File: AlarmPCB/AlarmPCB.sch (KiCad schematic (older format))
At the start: 13 parts

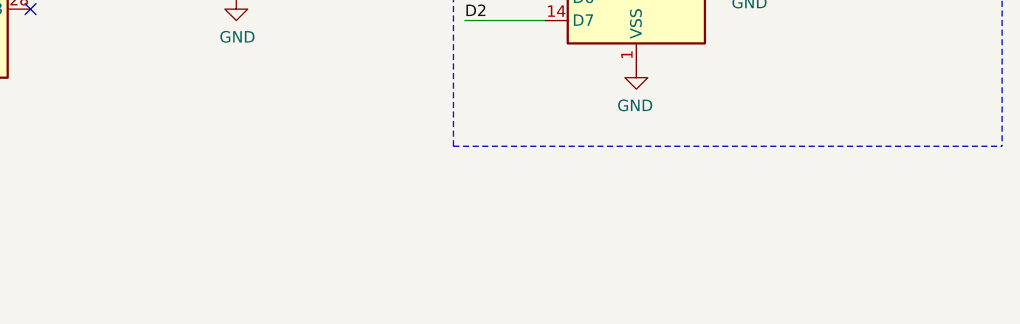
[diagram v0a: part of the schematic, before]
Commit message: Updated PCB GND Layer
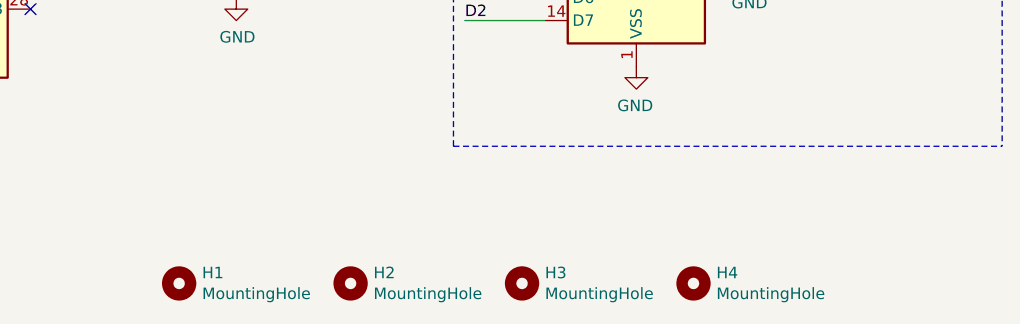
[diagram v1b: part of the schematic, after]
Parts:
- added H1, H2, H3, H4: MountingHole, MountingHole:MountingHole_3.2mm_M3, symbol Mechanical:MountingHole
- PB1: footprint Button_Switch_THT:SW_TH_Tactile_Omron_B3F-10xx -> Button_Switch_THT:SW_PUSH-12mm_Wuerth-430476085716
- PB2, PB3: footprint Button_Switch_THT:Push_E-Switch_KS01Q01 -> Button_Switch_THT:SW_TH_Tactile_Omron_B3F-10xx
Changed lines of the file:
@@
 EESchema Schematic File Version 4
-LIBS:AlarmPCB-cache
 EELAYER 30 0
 EELAYER END
@@
 F 0 "PB3" V 1900 3900 50  0000 C CNN
 F 1 "CancelAlarm" H 1500 3850 50  0000 C CNN
-F 2 "Button_Switch_THT:Push_E-Switch_KS01Q01" H 1750 3950 50  0001 C CNN
+F 2 "Button_Switch_THT:SW_TH_Tactile_Omron_B3F-10xx" H 1750 3950 50  0001 C CNN
 F 3 "~" H 1750 3950 50  0001 C CNN
 	1    1750 3750
@@
 F 0 "PB2" V 1500 3850 50  0000 C CNN
 F 1 "Snooze" H 1200 3850 50  0000 C CNN
-F 2 "Button_Switch_THT:Push_E-Switch_KS01Q01" H 1350 3950 50  0001 C CNN
+F 2 "Button_Switch_THT:SW_TH_Tactile_Omron_B3F-10xx" H 1350 3950 50  0001 C CNN
 F 3 "~" H 1350 3950 50  0001 C CNN
 	1    1350 3750
@@
 F 0 "PB1" V 1150 3850 50  0000 C CNN
 F 1 "Backlight" H 800 3850 50  0000 C CNN
-F 2 "Button_Switch_THT:SW_TH_Tactile_Omron_B3F-10xx" H 1000 3950 50  0001 C CNN
+F 2 "Button_Switch_THT:SW_PUSH-12mm_Wuerth-430476085716" H 1000 3950 50  0001 C CNN
 F 3 "~" H 1000 3950 50  0001 C CNN
 	1    1000 3750
@@
 NoConn ~ 8000 4100
 NoConn ~ 8000 4200
+$Comp
+L Mechanical:MountingHole H1
+U 1 1 5F1B765B
+P 6400 5750
+F 0 "H1" H 6500 5796 50  0000 L CNN
+F 1 "MountingHole" H 6500 5705 50  0000 L CNN
+F 2 "MountingHole:MountingHole_3.2mm_M3" H 6400 5750 50  0001 C CNN
+F 3 "~" H 6400 5750 50  0001 C CNN
+	1    6400 5750
+	1    0    0    -1
+$EndComp
+$Comp
+L Mechanical:MountingHole H2
+U 1 1 5F1B83F1
+P 7150 5750
+F 0 "H2" H 7250 5796 50  0000 L CNN
+F 1 "MountingHole" H 7250 5705 50  0000 L CNN
+F 2 "MountingHole:MountingHole_3.2mm_M3" H 7150 5750 50  0001 C CNN
+F 3 "~" H 7150 5750 50  0001 C CNN
+	1    7150 5750
+	1    0    0    -1
+$EndComp
+$Comp
+L Mechanical:MountingHole H3
+U 1 1 5F1BA130
+P 7900 5750
+F 0 "H3" H 8000 5796 50  0000 L CNN
+F 1 "MountingHole" H 8000 5705 50  0000 L CNN
+F 2 "MountingHole:MountingHole_3.2mm_M3" H 7900 5750 50  0001 C CNN
+F 3 "~" H 7900 5750 50  0001 C CNN
+	1    7900 5750
+	1    0    0    -1
+$EndComp
+$Comp
+L Mechanical:MountingHole H4
+U 1 1 5F1BA136
+P 8650 5750
+F 0 "H4" H 8750 5796 50  0000 L CNN
+F 1 "MountingHole" H 8750 5705 50  0000 L CNN
+F 2 "MountingHole:MountingHole_3.2mm_M3" H 8650 5750 50  0001 C CNN
+F 3 "~" H 8650 5750 50  0001 C CNN
+	1    8650 5750
+	1    0    0    -1
+$EndComp
 $EndSCHEMATC

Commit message: PCB Dimensions
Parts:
- PB1: footprint Button_Switch_THT:SW_PUSH-12mm_Wuerth-430476085716 -> Connector_PinHeader_2.54mm:PinHeader_1x03_P2.54mm_Vertical
- PB2, PB3: footprint Button_Switch_THT:SW_TH_Tactile_Omron_B3F-10xx -> Connector_PinHeader_2.54mm:PinHeader_1x02_P2.54mm_Vertical
- R1: footprint OptoDevice:R_LDR_4.9x4.2mm_P2.54mm_Vertical -> Connector_PinHeader_2.54mm:PinHeader_1x02_P2.54mm_Vertical
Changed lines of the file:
@@
 F 0 "PB3" V 1900 3900 50  0000 C CNN
 F 1 "CancelAlarm" H 1500 3850 50  0000 C CNN
-F 2 "Button_Switch_THT:SW_TH_Tactile_Omron_B3F-10xx" H 1750 3950 50  0001 C CNN
+F 2 "Connector_PinHeader_2.54mm:PinHeader_1x02_P2.54mm_Vertical" H 1750 3950 50  0001 C CNN
 F 3 "~" H 1750 3950 50  0001 C CNN
 	1    1750 3750
@@
 F 0 "PB2" V 1500 3850 50  0000 C CNN
 F 1 "Snooze" H 1200 3850 50  0000 C CNN
-F 2 "Button_Switch_THT:SW_TH_Tactile_Omron_B3F-10xx" H 1350 3950 50  0001 C CNN
+F 2 "Connector_PinHeader_2.54mm:PinHeader_1x02_P2.54mm_Vertical" H 1350 3950 50  0001 C CNN
 F 3 "~" H 1350 3950 50  0001 C CNN
 	1    1350 3750
@@
 F 0 "PB1" V 1150 3850 50  0000 C CNN
 F 1 "Backlight" H 800 3850 50  0000 C CNN
-F 2 "Button_Switch_THT:SW_PUSH-12mm_Wuerth-430476085716" H 1000 3950 50  0001 C CNN
+F 2 "Connector_PinHeader_2.54mm:PinHeader_1x03_P2.54mm_Vertical" H 1000 3950 50  0001 C CNN
 F 3 "~" H 1000 3950 50  0001 C CNN
 	1    1000 3750
@@
 F 0 "R1" V 4150 2950 50  0000 L CNN
 F 1 "PhotoResistor" V 4250 2800 50  0000 L CNN
-F 2 "OptoDevice:R_LDR_4.9x4.2mm_P2.54mm_Vertical" V 4100 2750 50  0001 L CNN
+F 2 "Connector_PinHeader_2.54mm:PinHeader_1x02_P2.54mm_Vertical" V 4100 2750 50  0001 L CNN
 F 3 "~" H 4050 2950 50  0001 C CNN
 	1    4050 3000

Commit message: Updated Pot footprint
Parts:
- RV1: footprint Potentiometer_THT:Potentiometer_ACP_CA6-H2,5_Horizontal -> digikey-footprints:Potentiometer_P120PK-Y25BR10K
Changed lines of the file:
@@
 EESchema Schematic File Version 4
+LIBS:AlarmPCB-cache
 EELAYER 30 0
 EELAYER END
@@
 F 0 "RV1" V 9300 3450 50  0000 R CNN
 F 1 "Contrast" H 9350 3550 50  0000 R CNN
-F 2 "Potentiometer_THT:Potentiometer_ACP_CA6-H2,5_Horizontal" H 9400 3400 50  0001 C CNN
+F 2 "digikey-footprints:Potentiometer_P120PK-Y25BR10K" H 9400 3400 50  0001 C CNN
 F 3 "~" H 9400 3400 50  0001 C CNN
 	1    9400 3400

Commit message: PCB rev
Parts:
- PB1: footprint Connector_PinHeader_2.54mm:PinHeader_1x03_P2.54mm_Vertical -> Button_Switch_THT:SW_TH_Tactile_Omron_B3F-10xx
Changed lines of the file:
@@
 EESchema Schematic File Version 4
-LIBS:AlarmPCB-cache
 EELAYER 30 0
 EELAYER END
@@
 F 0 "PB1" V 1150 3850 50  0000 C CNN
 F 1 "Backlight" H 800 3850 50  0000 C CNN
-F 2 "Connector_PinHeader_2.54mm:PinHeader_1x03_P2.54mm_Vertical" H 1000 3950 50  0001 C CNN
+F 2 "Button_Switch_THT:SW_TH_Tactile_Omron_B3F-10xx" H 1000 3950 50  0001 C CNN
 F 3 "~" H 1000 3950 50  0001 C CNN
 	1    1000 3750

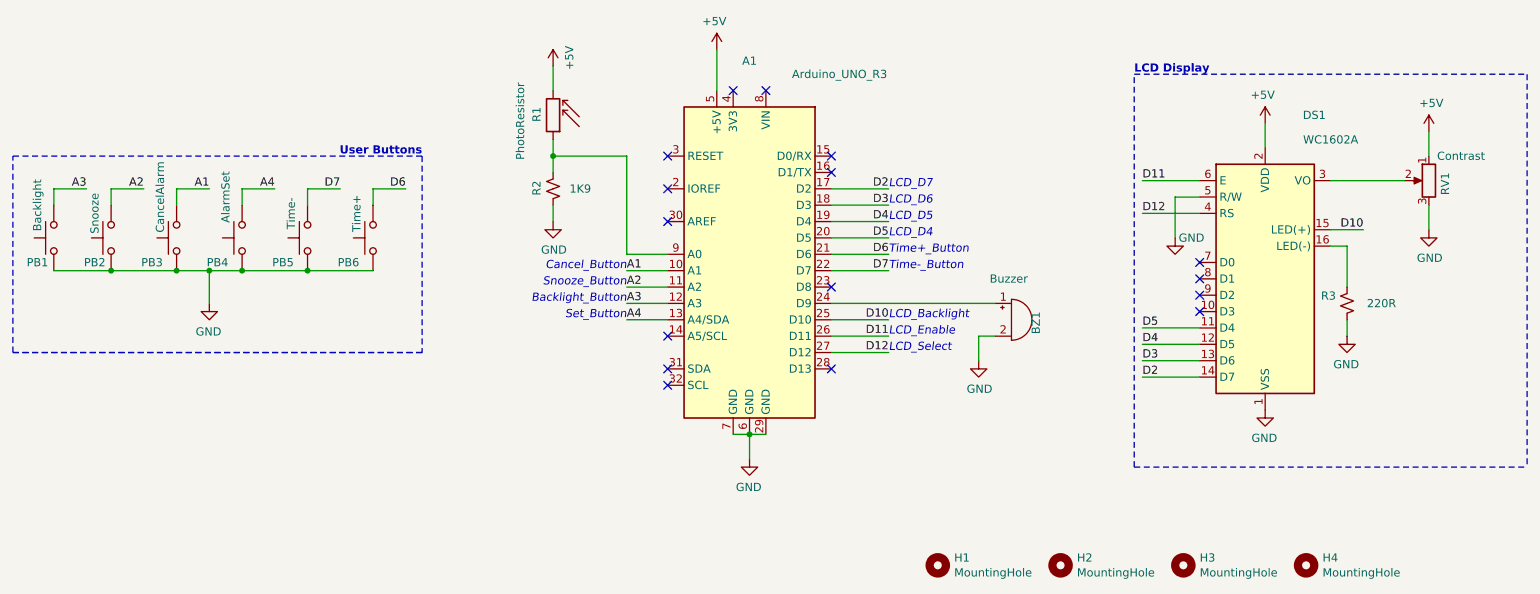
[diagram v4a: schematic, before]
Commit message: Updated Resistor Values
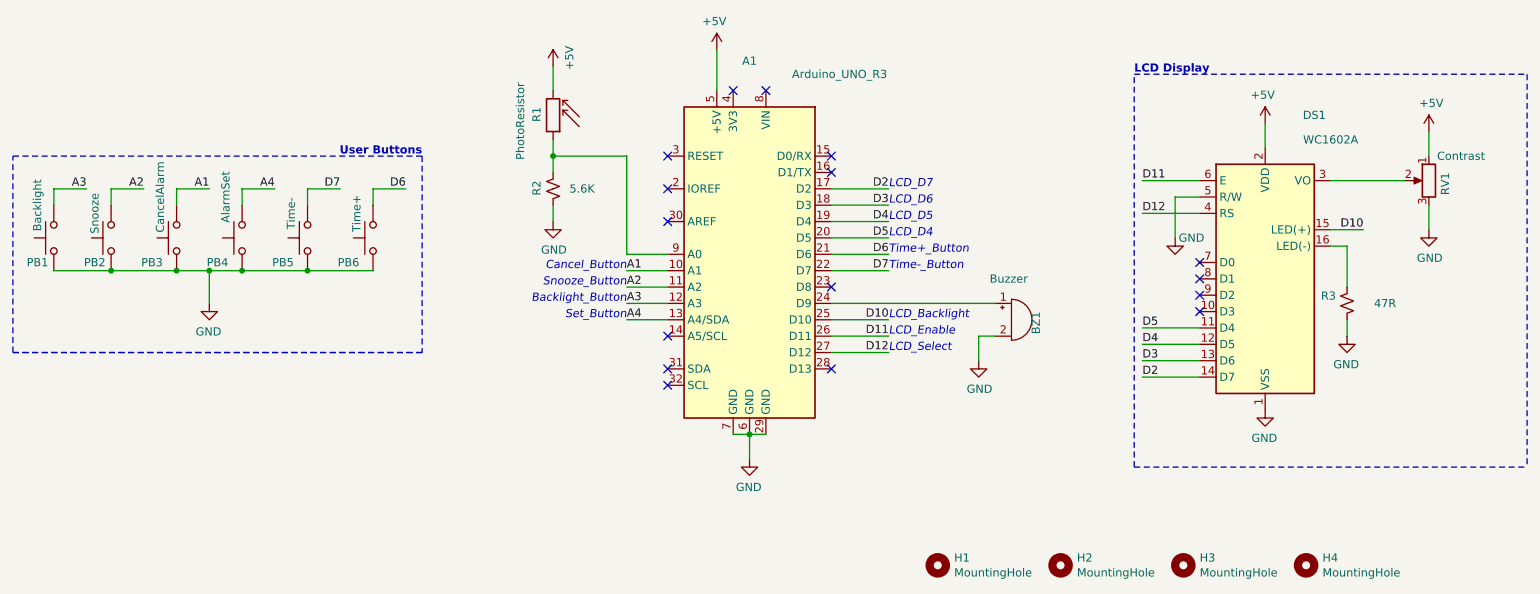
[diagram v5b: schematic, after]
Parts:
- R2: value 1K9 -> 5.6K
- R3: value 220R -> 47R
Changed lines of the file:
@@
 EESchema Schematic File Version 4
+LIBS:AlarmPCB-cache
 EELAYER 30 0
 EELAYER END
@@
 P 8900 4150
 F 0 "R3" H 8968 4196 50  0000 L CNN
-F 1 "220R" H 8600 4150 50  0000 L CNN
+F 1 "47R" H 8600 4150 50  0000 L CNN
 F 2 "Resistor_THT:R_Axial_DIN0309_L9.0mm_D3.2mm_P12.70mm_Horizontal" H 8900 4150 50  0001 C CNN
 F 3 "~" H 8900 4150 50  0001 C CNN
@@
 P 4050 3450
 F 0 "R2" V 3950 3400 50  0000 L CNN
-F 1 "1K9" H 4150 3450 50  0000 L CNN
+F 1 "5.6K" H 4150 3450 50  0000 L CNN
 F 2 "Resistor_THT:R_Axial_DIN0309_L9.0mm_D3.2mm_P12.70mm_Horizontal" H 4050 3450 50  0001 C CNN
 F 3 "~" H 4050 3450 50  0001 C CNN
